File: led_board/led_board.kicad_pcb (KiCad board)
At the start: 2 copper layers, 26 x 10.5 mm, 6 parts, among them J1 Conn_01x03, J2 Conn_01x02, J3 Conn_01x02, J4 Conn_01x02

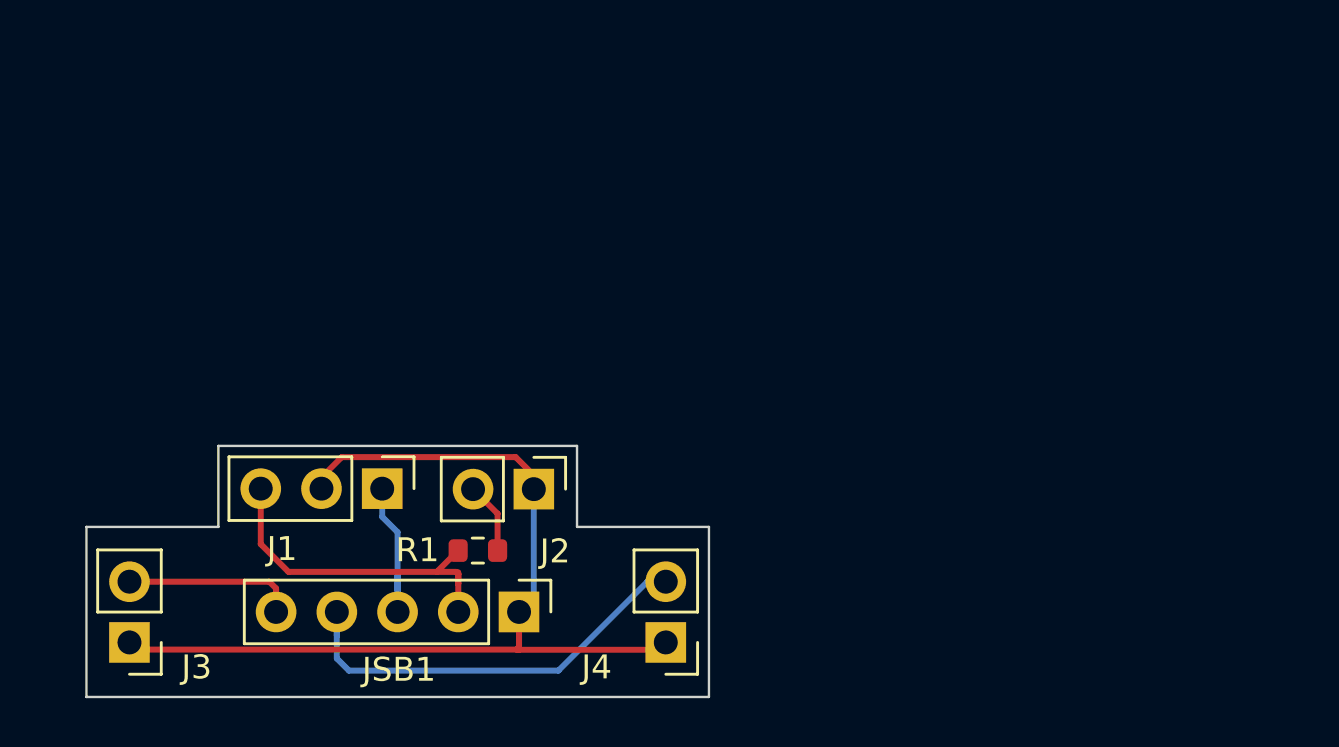
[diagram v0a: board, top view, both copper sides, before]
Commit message: feat(board): modify board outline
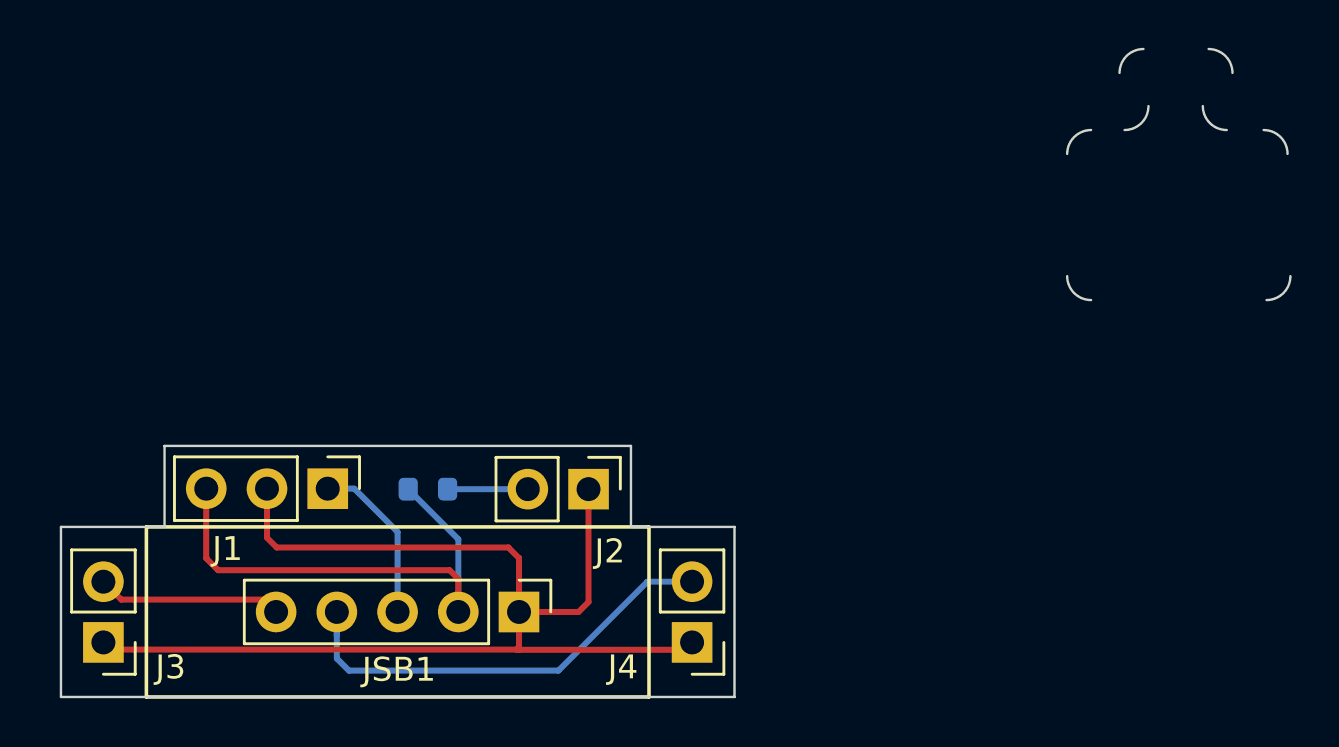
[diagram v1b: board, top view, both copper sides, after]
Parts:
- R1: moved to B.Cu
- moved R1 3.31 mm to (114.3, 98.4)
- moved J2 2.29 mm to (121.0, 98.4)
- moved J1 2.28 mm to (110.1, 98.4)
- moved J4 1.10 mm to (125.3, 104.8)
- moved J3 1.09 mm to (100.7, 104.8)
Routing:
- net +3.3V: track 41.9 -> 51.8 mm
- net GND: track 15.0 -> 21.8 mm
- net /T: track 18.4 -> 19.5 mm
- net /F: track 7.72 -> 8.73 mm
- net /HL: track 2.99 -> 3.93 mm
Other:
- board size 26 x 10.5 mm -> 51.4 x 27.1 mm

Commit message: feat(board): modify board outline
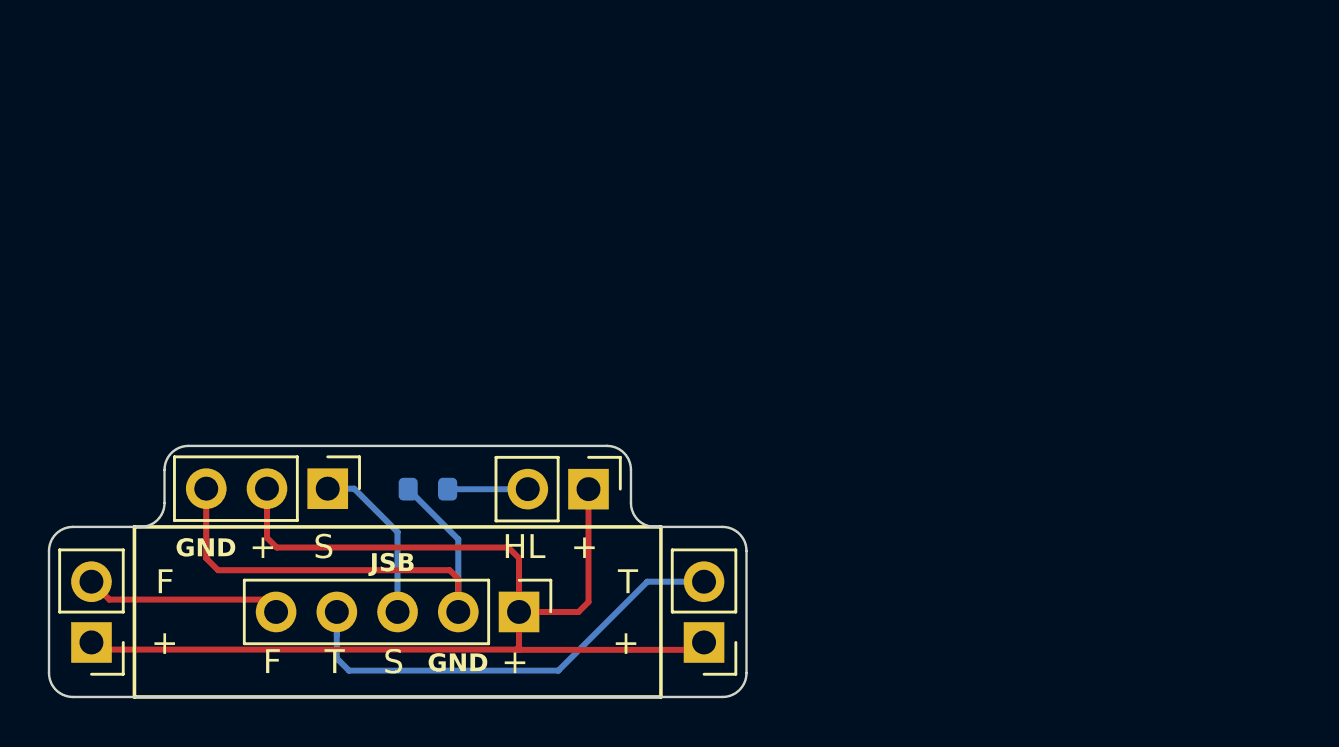
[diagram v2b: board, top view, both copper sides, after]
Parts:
- moved J3 0.50 mm to (100.2, 104.8)
- moved J4 0.50 mm to (125.8, 104.8)
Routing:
- net +3.3V: track 51.8 -> 53.3 mm
- net /T: track 19.5 -> 20.0 mm
- net /F: track 8.73 -> 9.23 mm
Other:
- board size 51.4 x 27.1 mm -> 29.2 x 10.5 mm
- board text added: "+"
- board text added: "F"
- board text added: "GND"
- board text added: "HL"
- board text added: "JSB"
- board text added: "S"
- board text added: "T"

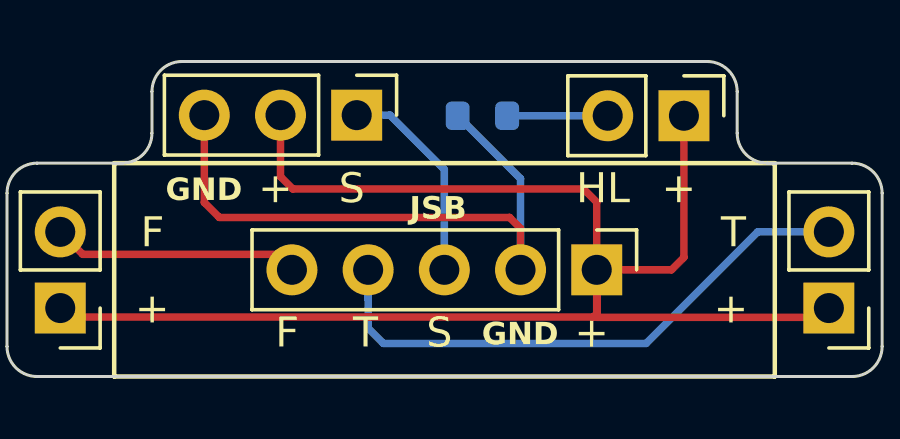
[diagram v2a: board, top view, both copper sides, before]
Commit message: feat: modify logo
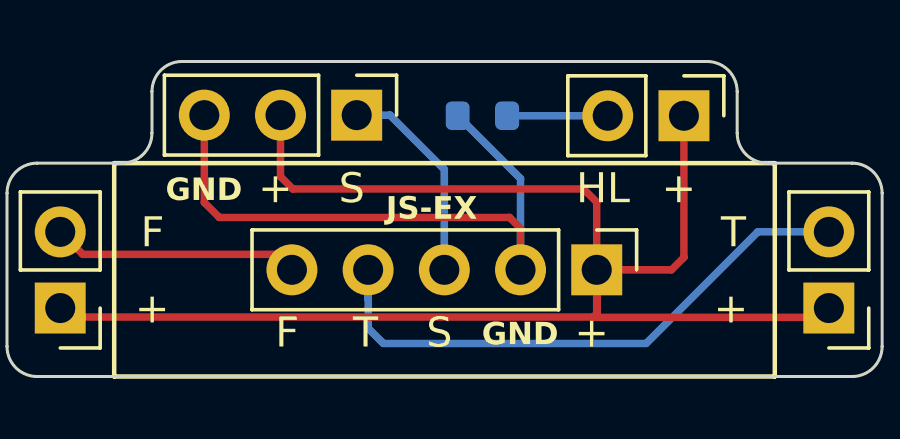
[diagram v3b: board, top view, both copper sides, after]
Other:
- board text added: "JS-EX"
- board text removed: "JSB"
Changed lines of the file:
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@@
       (layer "F.SilkS" (type "Top Silk Screen"))
       (layer "F.Paste" (type "Top Solder Paste"))
-      (layer "F.Mask" (type "Top Solder Mask") (color "Blue") (thickness 0.01))
+      (layer "F.Mask" (type "Top Solder Mask") (color "Black") (thickness 0.01))
       (layer "F.Cu" (type "copper") (thickness 0.035))
       (layer "dielectric 1" (type "core") (thickness 0.71) (material "FR4") (epsilon_r 4.5) (loss_tangent 0.02))
       (layer "B.Cu" (type "copper") (thickness 0.035))
-      (layer "B.Mask" (type "Bottom Solder Mask") (color "Blue") (thickness 0.01))
+      (layer "B.Mask" (type "Bottom Solder Mask") (color "Black") (thickness 0.01))
       (layer "B.Paste" (type "Bottom Solder Paste"))
       (layer "B.SilkS" (type "Bottom Silk Screen"))
@@
     (effects (font (size 1 1) (thickness 0.15)) (justify left bottom mirror))
   )
-  (gr_text "JSB" (at 113.86 101.95) (layer "B.SilkS")
+  (gr_text "JS-EX" (at 114.971072 101.95) (layer "B.SilkS")
     (effects (font (size 0.75 0.75) (thickness 0.15) bold) (justify left bottom mirror))
   )
@@
     (effects (font (size 1 1) (thickness 0.15)) (justify left bottom))
   )
-  (gr_text "JSB" (at 111.849643 101.94) (layer "F.SilkS")
+  (gr_text "JS-EX" (at 111.063929 101.94) (layer "F.SilkS")
     (effects (font (size 0.75 0.75) (thickness 0.15) bold) (justify left bottom))
   )
